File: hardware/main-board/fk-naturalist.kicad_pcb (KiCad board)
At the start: 2 copper layers, 103 x 37.5 mm, 127 parts, among them J1 RF-SMA-EDGE, J10 S2B-PH-SM4-TB, J11 RF-SMA-EDGE, J12 CONN_01x02, J13 CONN_01x06, J14 CONN_01x02, J2 CONN_01x02, J3 S2B-PH-SM4-TB, J4 Conn_01x01, J5 CONN_01x03_SERIAL, J6 CONN_01x09, J7 CONN_02x05_SWD, J8 CONN_01x02, J9 MICRO-USB, M10 FIDUCIAL, M11 FIDUCIAL, M2 FIDUCIAL, M5 FIDUCIAL, M7 MICRO-SD, M8 FIDUCIAL, M9 FIDUCIAL, Q1 2N7002LT1G, SW1 SPNO, SW2 SPNO, U1 ATWINC1500-MR210PA, U10 FGPMMOPA6H, U11 MAX1704XX, U12 TPS2052B, U13 SK6812, U14 MCP1700T-3302E/MB, U2 ATSAMD21G18A-AU, U3 RFM95W, U4 24AA02E64, U5 S25FL116K0XMFI041, U6 BQ24074RGTT, U7 PCF8523, U8 TL5209, U9 TL5209, Y1 FC-135, Y2 FC-135

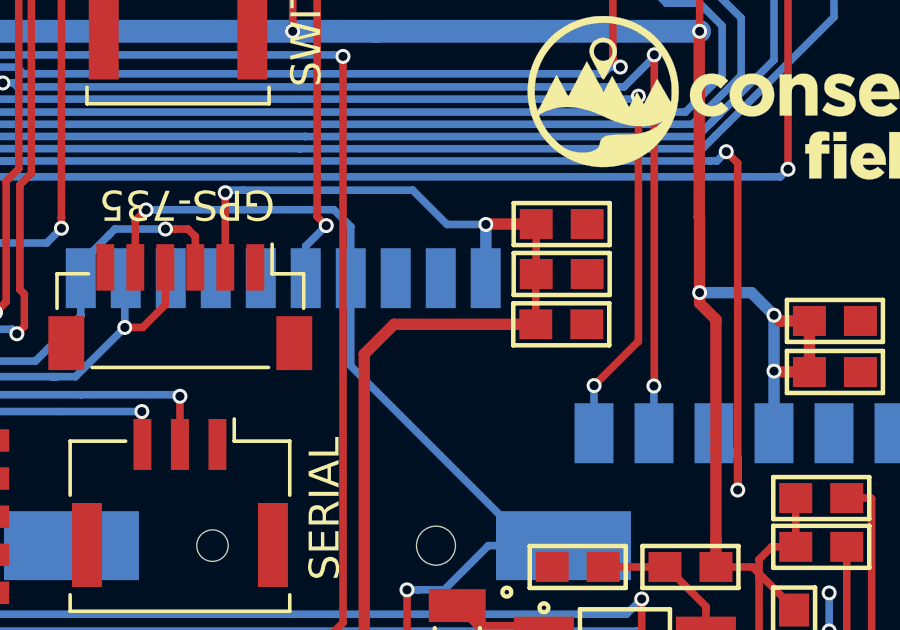
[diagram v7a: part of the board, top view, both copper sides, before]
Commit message: Add a bead on the GPS 3v3 supply too.
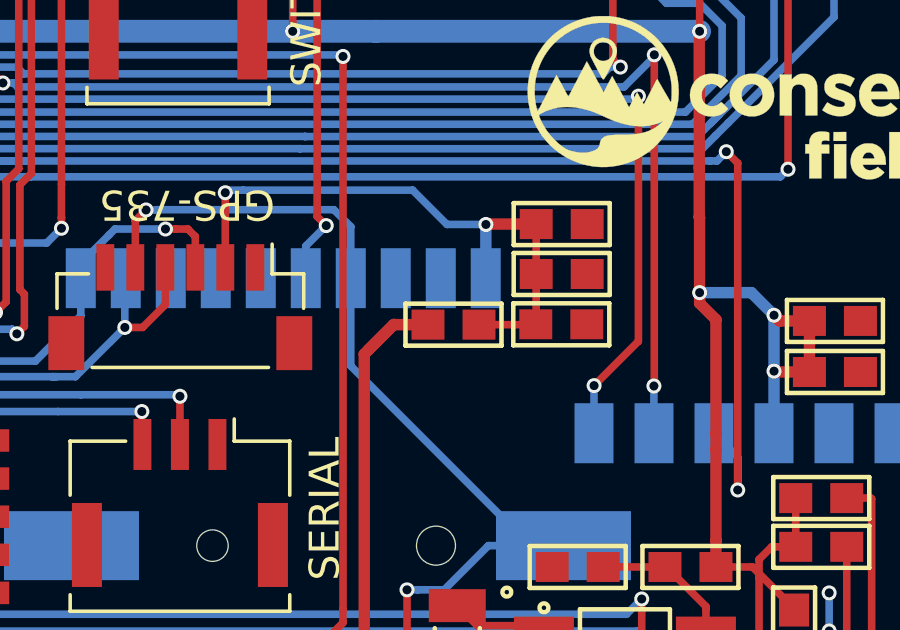
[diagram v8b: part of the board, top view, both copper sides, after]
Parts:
- added L3: BLM18KG221SN1D, conservify:IND-0603, F.Cu at (151.7, 131.4)
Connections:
- C31 pad 2: /GPS_3V3 -> Net-(C31-Pad2)
- C32 pad 1: /GPS_3V3 -> Net-(C31-Pad2)
- C35 pad 1: /GPS_3V3 -> Net-(C31-Pad2)
- J13 pad 2: /GPS_3V3 -> Net-(C31-Pad2)
- U10 pad 1: /GPS_3V3 -> Net-(C31-Pad2)
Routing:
- net /GPS_3V3: track 76.7 -> 55.2 mm, vias 4 -> 2
- net Net-(C31-Pad2): track 0.00 -> 21.1 mm, vias 0 -> 2
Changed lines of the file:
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@@
     (thickness 1.6)
     (drawings 28)
-    (tracks 1611)
+    (tracks 1616)
     (zones 0)
-    (modules 127)
-    (nets 134)
+    (modules 128)
+    (nets 135)
   )
   (page A4)
@@
   )
   (setup
-    (last_trace_width 0.254)
+    (last_trace_width 0.381)
     (user_trace_width 0.2032)
     (user_trace_width 0.254)
@@
   (net 132 /I2S_WS)
   (net 133 /I2S_DATA)
+  (net 134 "Net-(C31-Pad2)")
   (net_class Default "This is the default net class."
     (clearance 0.1524)
@@
     (add_net "Net-(C29-Pad1)")
     (add_net "Net-(C3-Pad2)")
+    (add_net "Net-(C31-Pad2)")
     (add_net "Net-(C4-Pad2)")
     (add_net "Net-(C6-Pad1)")
@@
     (fp_line (start -8.001 -8.001) (end -8.001 0) (layer B.SilkS) (width 0.381))
     (pad 1 smd rect (at -8.001 6.74878 90) (size 1.99898 1.00076) (layers B.Cu B.Paste B.Mask)
-      (net 109 /GPS_3V3))
+      (net 134 "Net-(C31-Pad2)"))
     (pad 2 smd rect (at -8.001 5.25018 90) (size 1.99898 1.00076) (layers B.Cu B.Paste B.Mask)
       (net 79 "Net-(U10-Pad2)"))
@@
       (net 1 GND))
     (pad 2 smd rect (at -1.5 1.325 180) (size 0.6 1.55) (layers F.Cu F.Paste F.Mask)
-      (net 109 /GPS_3V3))
+      (net 134 "Net-(C31-Pad2)"))
     (pad 3 smd rect (at -0.5 1.325 180) (size 0.6 1.55) (layers F.Cu F.Paste F.Mask)
       (net 90 /GPS_RX))
@@
       (net 1 GND))
     (pad 2 smd rect (at 0.85 0 180) (size 1.1 1) (layers F.Cu F.Paste F.Mask)
-      (net 109 /GPS_3V3))
+      (net 134 "Net-(C31-Pad2)"))
     (model RocketScreamKicadLibrary.3dshapes/CAP-0603.wrl
       (at (xyz 0 0 0))
@@
     (fp_line (start 1.6 0.7) (end -1.6 0.7) (layer F.SilkS) (width 0.15))
     (pad 1 smd rect (at -0.85 0) (size 1.1 1) (layers F.Cu F.Paste F.Mask)
-      (net 109 /GPS_3V3))
+      (net 134 "Net-(C31-Pad2)"))
     (pad 2 smd rect (at 0.85 0) (size 1.1 1) (layers F.Cu F.Paste F.Mask)
       (net 1 GND))
@@
       (net 1 GND))
     (pad 1 smd rect (at -0.85 0) (size 1.1 1) (layers F.Cu F.Paste F.Mask)
-      (net 109 /GPS_3V3))
+      (net 134 "Net-(C31-Pad2)"))
     (model RocketScreamKicadLibrary.3dshapes/CAP-0603.wrl
       (at (xyz 0 0 0))
@@
     )
   )
+  (module conservify:IND-0603 (layer F.Cu)
+    (at 151.6888 131.445)
+    (descr "Inductor SMD 0603")
+    (tags "Inductor 0603")
+    (attr smd)
+    (fp_text reference L3 (at 0 -1.9) (layer F.SilkS) hide
+      (effects (font (size 1 1) (thickness 0.15)))
+    )
+    (fp_text value BLM18KG221SN1D (at 0 1.9) (layer F.Fab)
+      (effects (font (size 1 1) (thickness 0.15)))
+    )
+    (fp_line (start 1.65 -0.75) (end -1.65 -0.75) (layer F.CrtYd) (width 0.05))
+    (fp_line (start -1.65 -0.75) (end -1.65 0.75) (layer F.CrtYd) (width 0.05))
+    (fp_line (start -1.65 0.75) (end 1.65 0.75) (layer F.CrtYd) (width 0.05))
+    (fp_line (start 1.65 0.75) (end 1.65 -0.75) (layer F.CrtYd) (width 0.05))
+    (fp_line (start -1.6 -0.7) (end -1.6 0.7) (layer F.SilkS) (width 0.15))
+    (fp_line (start 1.6 -0.7) (end 1.6 0.7) (layer F.SilkS) (width 0.15))
+    (fp_line (start -1.6 -0.7) (end 1.6 -0.7) (layer F.SilkS) (width 0.15))
+    (fp_line (start 1.6 0.7) (end -1.6 0.7) (layer F.SilkS) (width 0.15))
+    (pad 1 smd rect (at -0.85 0) (size 1.1 1) (layers F.Cu F.Paste F.Mask)
+      (net 109 /GPS_3V3))
+    (pad 2 smd rect (at 0.85 0) (size 1.1 1) (layers F.Cu F.Paste F.Mask)
+      (net 134 "Net-(C31-Pad2)"))
+    (model Capacitors_SMD.3dshapes/C_0603.wrl
+      (at (xyz 0 0 0))
+      (scale (xyz 1 1 1))
+      (rotate (xyz 0 0 0))
+    )
+  )
   (gr_text PERIPH_3V3 (at 115.2271 143.9672 270) (layer B.SilkS)
     (effects (font (size 0.5 0.5) (thickness 0.1)) (justify mirror))
@@
   (segment (start 122.294522 143.440022) (end 122.936 144.0815) (width 0.381) (layer F.Cu) (net 109))
   (via (at 122.936 144.0815) (size 0.5) (drill 0.3) (layers F.Cu B.Cu) (net 109))
-  (segment (start 152.7175 129.94132) (end 152.76322 129.8956) (width 0.254) (layer B.Cu) (net 109))
+  (segment (start 152.7175 129.94132) (end 152.76322 129.8956) (width 0.254) (layer B.Cu) (net 134))
   (via (at 148.463 142.3035) (size 0.5) (drill 0.3) (layers F.Cu B.Cu) (net 109))
   (segment (start 120.725006 145.288) (end 120.3071 145.288) (width 0.381) (layer B.Cu) (net 109))
@@
   (segment (start 119.5705 140.147) (end 119.5705 142.937324) (width 0.381) (layer F.Cu) (net 109))
   (segment (start 119.5705 142.937324) (end 120.073198 143.440022) (width 0.381) (layer F.Cu) (net 109))
-  (segment (start 152.6794 129.81178) (end 152.76322 129.8956) (width 0.254) (layer B.Cu) (net 109))
-  (segment (start 152.76322 129.39649) (end 152.76322 129.8956) (width 0.254) (layer B.Cu) (net 109))
-  (segment (start 144.676353 126.9619) (end 150.32863 126.9619) (width 0.254) (layer B.Cu) (net 109))
-  (segment (start 144.1664 126.9619) (end 144.0815 127.0468) (width 0.254) (layer B.Cu) (net 109))
-  (via (at 144.0815 127.0468) (size 0.5) (drill 0.3) (layers F.Cu B.Cu) (net 109))
-  (segment (start 144.676353 126.9619) (end 144.1664 126.9619) (width 0.254) (layer B.Cu) (net 109))
-  (segment (start 144.0815 129.5344) (end 144.0829 129.5358) (width 0.254) (layer F.Cu) (net 109))
-  (segment (start 144.0815 127.0468) (end 144.0815 129.5344) (width 0.254) (layer F.Cu) (net 109))
+  (segment (start 152.6794 129.81178) (end 152.76322 129.8956) (width 0.254) (layer B.Cu) (net 134))
+  (segment (start 152.76322 129.39649) (end 152.76322 129.8956) (width 0.254) (layer B.Cu) (net 134))
+  (segment (start 144.676353 126.9619) (end 150.32863 126.9619) (width 0.254) (layer B.Cu) (net 134))
+  (segment (start 144.1664 126.9619) (end 144.0815 127.0468) (width 0.254) (layer B.Cu) (net 134))
+  (via (at 144.0815 127.0468) (size 0.5) (drill 0.3) (layers F.Cu B.Cu) (net 134))
+  (segment (start 144.676353 126.9619) (end 144.1664 126.9619) (width 0.254) (layer B.Cu) (net 134))
+  (segment (start 144.0815 129.5344) (end 144.0829 129.5358) (width 0.254) (layer F.Cu) (net 134))
+  (segment (start 144.0815 127.0468) (end 144.0815 129.5344) (width 0.254) (layer F.Cu) (net 134))
   (segment (start 122.936 144.0815) (end 127.3937 144.0815) (width 0.381) (layer B.Cu) (net 109))
   (segment (start 129.1717 142.3035) (end 127.3937 144.0815) (width 0.381) (layer B.Cu) (net 109))
@@
   (segment (start 148.712999 142.053501) (end 148.712999 132.426901) (width 0.381) (layer F.Cu) (net 109))
   (segment (start 148.463 142.3035) (end 148.712999 142.053501) (width 0.381) (layer F.Cu) (net 109))
-  (segment (start 149.706699 131.433201) (end 154.431501 131.433201) (width 0.381) (layer F.Cu) (net 109))
-  (segment (start 148.712999 132.426901) (end 149.706699 131.433201) (width 0.381) (layer F.Cu) (net 109))
-  (via (at 152.7683 128.1049) (size 0.5) (drill 0.3) (layers F.Cu B.Cu) (net 109))
-  (segment (start 152.781 128.0922) (end 152.7683 128.1049) (width 0.381) (layer F.Cu) (net 109))
-  (segment (start 154.4456 128.0922) (end 152.781 128.0922) (width 0.381) (layer F.Cu) (net 109))
-  (segment (start 152.7683 129.89052) (end 152.76322 129.8956) (width 0.381) (layer B.Cu) (net 109))
-  (segment (start 152.7683 128.1049) (end 152.7683 129.89052) (width 0.381) (layer B.Cu) (net 109))
-  (segment (start 154.4456 128.0922) (end 154.4456 129.7559) (width 0.254) (layer F.Cu) (net 109))
-  (segment (start 154.431501 129.769999) (end 154.4456 129.7559) (width 0.254) (layer F.Cu) (net 109))
-  (segment (start 154.431501 131.433201) (end 154.431501 129.769999) (width 0.254) (layer F.Cu) (net 109))
-  (segment (start 151.47163 128.1049) (end 150.32863 126.9619) (width 0.254) (layer B.Cu) (net 109))
-  (segment (start 152.7683 128.1049) (end 151.47163 128.1049) (width 0.254) (layer B.Cu) (net 109))
+  (segment (start 149.6949 131.445) (end 148.844 132.2959) (width 0.381) (layer F.Cu) (net 109))
+  (segment (start 150.8388 131.445) (end 149.6949 131.445) (width 0.381) (layer F.Cu) (net 109))
+  (segment (start 148.844 132.2959) (end 149.706699 131.433201) (width 0.381) (layer F.Cu) (net 109))
+  (segment (start 148.712999 132.426901) (end 148.844 132.2959) (width 0.381) (layer F.Cu) (net 109))
+  (via (at 152.7683 128.1049) (size 0.5) (drill 0.3) (layers F.Cu B.Cu) (net 134))
+  (segment (start 152.781 128.0922) (end 152.7683 128.1049) (width 0.381) (layer F.Cu) (net 134))
+  (segment (start 154.4456 128.0922) (end 152.781 128.0922) (width 0.381) (layer F.Cu) (net 134))
+  (segment (start 152.7683 129.89052) (end 152.76322 129.8956) (width 0.381) (layer B.Cu) (net 134))
+  (segment (start 152.7683 128.1049) (end 152.7683 129.89052) (width 0.381) (layer B.Cu) (net 134))
+  (segment (start 154.4456 128.0922) (end 154.4456 129.7559) (width 0.254) (layer F.Cu) (net 134))
+  (segment (start 154.431501 129.769999) (end 154.4456 129.7559) (width 0.254) (layer F.Cu) (net 134))
+  (segment (start 151.47163 128.1049) (end 150.32863 126.9619) (width 0.254) (layer B.Cu) (net 134))
+  (segment (start 152.7683 128.1049) (end 151.47163 128.1049) (width 0.254) (layer B.Cu) (net 134))
   (segment (start 117.0305 140.147) (end 117.0305 141.401) (width 0.254) (layer F.Cu) (net 110))
   (segment (start 117.0305 141.401) (end 116.255 142.1765) (width 0.254) (layer F.Cu) (net 110))
@@
   (segment (start 112.9157 117.0559) (end 114.5213 115.4503) (width 0.254) (layer F.Cu) (net 133))
   (segment (start 112.9157 122.4534) (end 112.9157 117.0559) (width 0.254) (layer F.Cu) (net 133))
+  (segment (start 154.419702 131.445) (end 154.431501 131.433201) (width 0.254) (layer F.Cu) (net 134))
+  (segment (start 152.5388 131.445) (end 154.419702 131.445) (width 0.254) (layer F.Cu) (net 134))
+  (segment (start 154.4456 131.419102) (end 154.431501 131.433201) (width 0.254) (layer F.Cu) (net 134))
+  (segment (start 154.4456 129.7559) (end 154.4456 131.419102) (width 0.254) (layer F.Cu) (net 134))
   (zone (net 1) (net_name GND) (layer B.Cu) (hatch edge 0.508)
     (connect_pads (clearance 0.2032))
